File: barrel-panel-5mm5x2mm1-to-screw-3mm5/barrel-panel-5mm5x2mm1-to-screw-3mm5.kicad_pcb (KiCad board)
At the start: 2 copper layers, 1 part, among them J1 Barrel_Jack

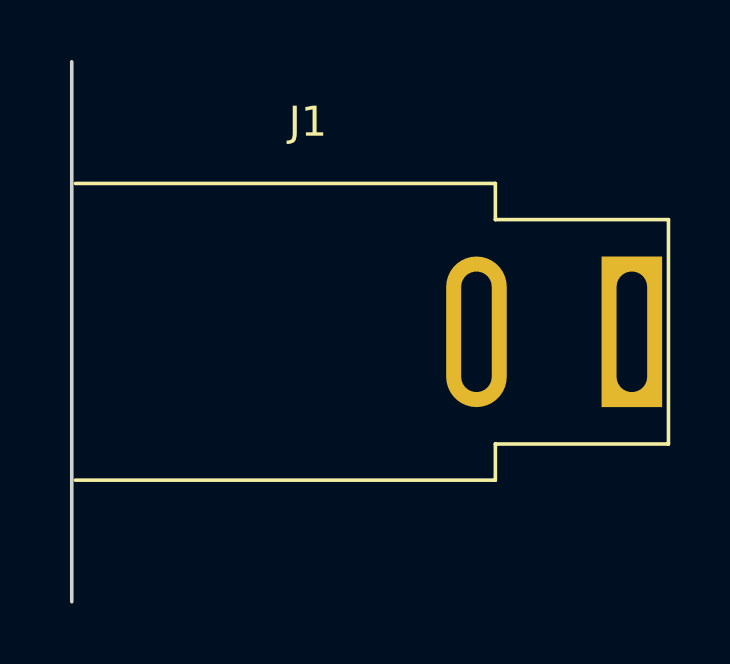
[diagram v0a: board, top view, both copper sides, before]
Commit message: some updates to barrel connector footprint
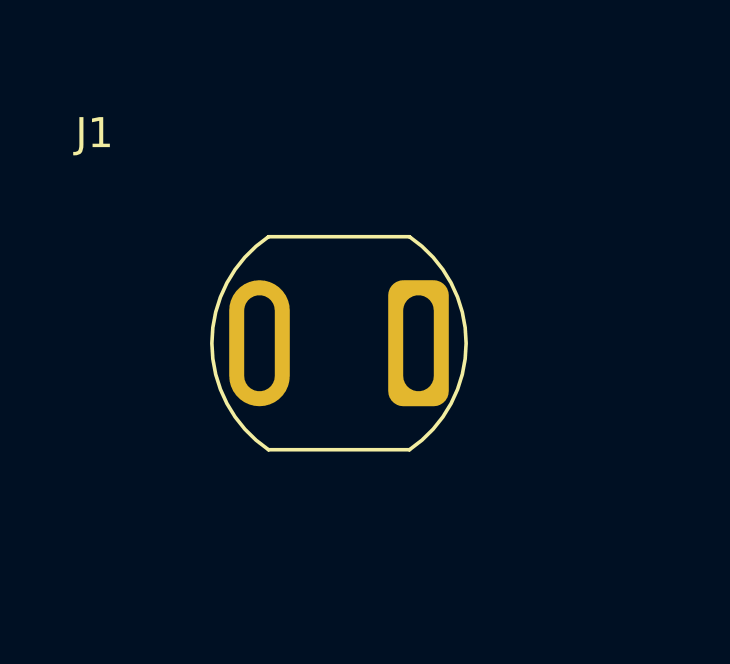
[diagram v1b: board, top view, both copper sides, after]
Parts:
- J1: footprint Connector_BarrelJack:BarrelJack_SwitchcraftConxall_RAPC10U_Horizontal -> Connector_Barreljack_panel:BarrelJack_panel_5.5mmx2.1mm_2_pins
- moved J1 7.12 mm to (154.3, 105.4)
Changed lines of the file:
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@@
   (net 1 "unconnected-(J1-Pad1)")
   (net 2 "unconnected-(J1-Pad2)")
-  (footprint "Connector_BarrelJack:BarrelJack_SwitchcraftConxall_RAPC10U_Horizontal" (layer "F.Cu")
-    (at 161.417 105.029)
+  (footprint "Connector_Barreljack_panel:BarrelJack_panel_5.5mmx2.1mm_2_pins" (layer "F.Cu")
+    (at 154.305 105.41)
     (descr "DC Power Jack, 13A, 24V, Panel Mount,Through-hole, https://www.switchcraft.com/Drawings/RAPC10U_CD.pdf")
     (tags "barreljack switchcraftconxall dc power")
@@
       (effects (font (size 1 1) (thickness 0.15)))
     )
-    (fp_line (start -4.55 -3.74) (end -4.55 -4.945) (layer "F.SilkS") (width 0.12))
-    (fp_line (start -4.55 3.74) (end 1.22 3.74) (layer "F.SilkS") (width 0.12))
-    (fp_line (start -4.55 4.945) (end -4.55 3.74) (layer "F.SilkS") (width 0.12))
-    (fp_line (start -18.55 4.945) (end -4.55 4.945) (layer "F.SilkS") (width 0.12))
-    (fp_line (start 1.22 -3.74) (end -4.55 -3.74) (layer "F.SilkS") (width 0.12))
-    (fp_line (start -4.55 -4.945) (end -18.55 -4.945) (layer "F.SilkS") (width 0.12))
-    (fp_line (start 1.22 3.74) (end 1.22 -3.74) (layer "F.SilkS") (width 0.12))
-    (fp_line (start -18.67 -9) (end -18.67 9) (layer "Edge.Cuts") (width 0.12))
-    (fp_line (start -28.93 -6.47) (end 1.51 -6.47) (layer "F.CrtYd") (width 0.05))
-    (fp_line (start 1.51 6.47) (end -28.93 6.47) (layer "F.CrtYd") (width 0.05))
-    (fp_line (start -28.93 6.47) (end -28.93 -6.47) (layer "F.CrtYd") (width 0.05))
-    (fp_line (start 1.51 -6.47) (end 1.51 6.47) (layer "F.CrtYd") (width 0.05))
-    (fp_line (start -20.17 -5.97) (end -18.77 -5.97) (layer "F.Fab") (width 0.1))
-    (fp_line (start 0 -3.62) (end -4.67 -3.62) (layer "F.Fab") (width 0.1))
-    (fp_line (start -18.77 -4.825) (end -4.67 -4.825) (layer "F.Fab") (width 0.1))
-    (fp_line (start -18.77 -5.97) (end -18.77 5.97) (layer "F.Fab") (width 0.1))
-    (fp_line (start -20.17 -5.97) (end -20.17 5.97) (layer "F.Fab") (width 0.1))
-    (fp_line (start -18.77 4.825) (end -4.67 4.825) (layer "F.Fab") (width 0.1))
-    (fp_line (start -4.67 -3.62) (end -4.67 -4.8) (layer "F.Fab") (width 0.1))
-    (fp_line (start -4.67 3.62) (end 0 3.62) (layer "F.Fab") (width 0.1))
-    (fp_line (start -4.67 4.8) (end -4.67 3.62) (layer "F.Fab") (width 0.1))
-    (fp_line (start -20.17 -4.065) (end -28.43 -4.065) (layer "F.Fab") (width 0.1))
-    (fp_line (start -28.43 3.175) (end -20.17 3.175) (layer "F.Fab") (width 0.1))
-    (fp_line (start -28.43 -4.065) (end -28.43 3.175) (layer "F.Fab") (width 0.1))
-    (fp_line (start -20.17 5.97) (end -18.77 5.97) (layer "F.Fab") (width 0.1))
-    (fp_line (start 0 3.62) (end 0 -3.62) (layer "F.Fab") (width 0.1))
-    (pad "1" thru_hole rect (at 0 0) (size 2.02 5.02) (drill oval 1.02 4.02) (layers *.Cu *.Mask)
+    (fp_line (start -5 -3.55) (end -0.3 -3.55) (layer "F.SilkS") (width 0.12))
+    (fp_line (start -5 3.55) (end -0.3 3.55) (layer "F.SilkS") (width 0.12))
+    (fp_arc (start -5 3.55) (mid -6.887569 0) (end -5 -3.55) (layer "F.SilkS") (width 0.12))
+    (fp_arc (start -0.3 -3.55) (mid 1.587569 0) (end -0.3 3.55) (layer "F.SilkS") (width 0.12))
+    (fp_circle (center -2.65 0) (end 1.75 0) (layer "F.CrtYd") (width 0.05) (fill none))
+    (fp_circle (center -2.65 0) (end 1.35 0) (layer "F.Fab") (width 0.1) (fill none))
+    (pad "1" thru_hole roundrect (at 0 0) (size 2.02 4.2) (drill oval 1.02 3.2) (layers *.Cu *.Mask) (roundrect_rratio 0.25)
       (net 1 "unconnected-(J1-Pad1)") (pintype "passive"))
-    (pad "2" thru_hole oval (at -5.18 0) (size 2.02 5.02) (drill oval 1.02 4.02) (layers *.Cu *.Mask)
+    (pad "2" thru_hole oval (at -5.3 0) (size 2.02 4.2) (drill oval 1.02 3.2) (layers *.Cu *.Mask)
       (net 2 "unconnected-(J1-Pad2)") (pintype "passive"))
     (model "${KICAD6_3DMODEL_DIR}/Connector_BarrelJack.3dshapes/BarrelJack_SwitchcraftConxall_RAPC10U_Horizontal.wrl"
